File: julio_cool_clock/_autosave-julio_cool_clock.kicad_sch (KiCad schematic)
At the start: 60 parts, among them J1 PJ-102AH, J2 Conn_02x03_Odd_Even, J3 Conn_01x06, Q1 NPN_2N3904_SOT23, SW1 Omron_B3F_SPST, SW2 Omron_B3F_SPST, SW3 Omron_B3F_SPST, SW4 Omron_B3F_SPST, U1 ATmega328-PU, U2 MAX7219, U3 DS1307_DIP-8, U4 L7805, Y1 Crystal_16MHz, Y2 Crystal_32768Hz

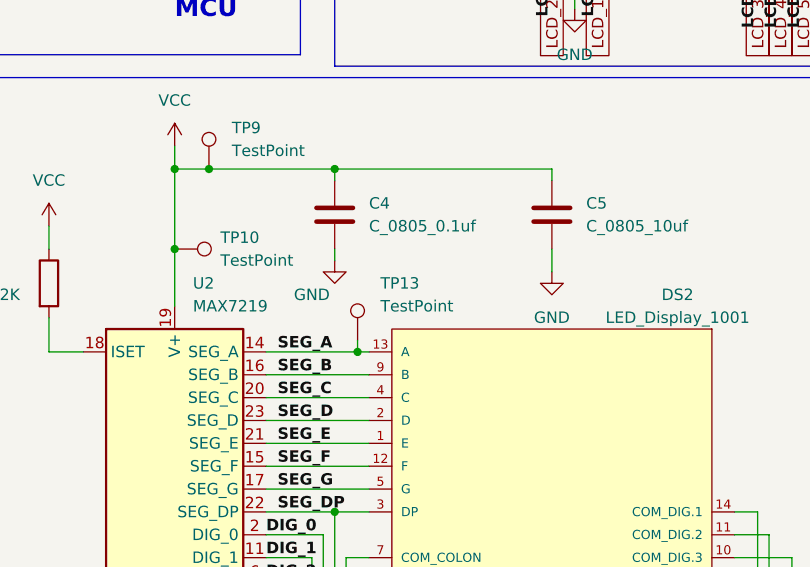
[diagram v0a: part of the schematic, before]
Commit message: Design Commit 6
Added prelim DFT features, completed PCB routing, and shipped first Gerber out.
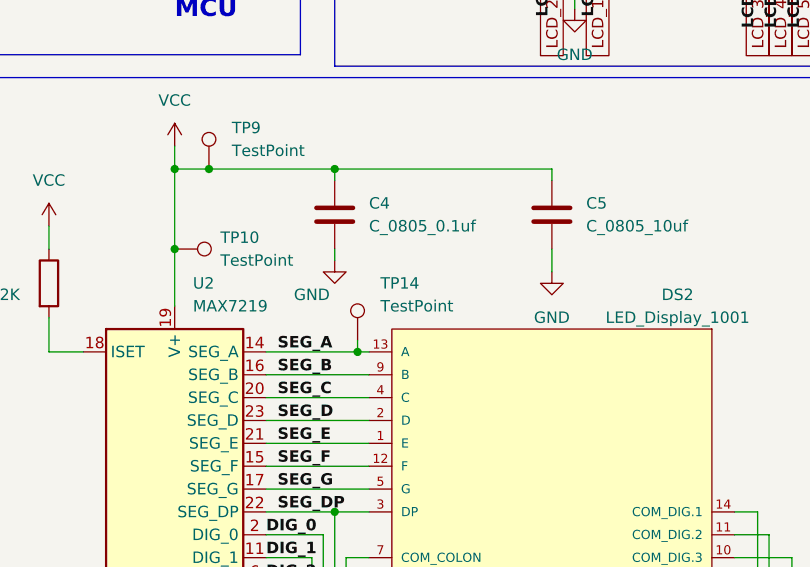
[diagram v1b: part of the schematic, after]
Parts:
- renumbered TP13 to TP14
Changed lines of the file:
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@@
   (symbol (lib_id "HPS:TestPoint") (at 113.03 143.51 0) (unit 1)
     (in_bom yes) (on_board yes)
-    (property "Reference" "TP13" (id 0) (at 115.57 137.16 0)
+    (property "Reference" "TP14" (id 0) (at 115.57 137.16 0)
       (effects (font (size 1.27 1.27)) (justify left))
     )
@@
       (reference "TP12") (unit 1) (value "TestPoint") (footprint "footprints:TestPoint_THTPad_D2.0mm_Drill1.0mm")
     )
-    (path "/18284de9-0621-4232-a79b-da0a3c7eb084"
-      (reference "TP13") (unit 1) (value "TestPoint") (footprint "footprints:TestPoint_THTPad_D2.0mm_Drill1.0mm")
-    )
     (path "/71840b63-43c6-4d29-b74e-3f6956efaa5c"
       (reference "TP13") (unit 1) (value "TestPoint") (footprint "footprints:TestPoint_THTPad_D2.0mm_Drill1.0mm")
     )
+    (path "/18284de9-0621-4232-a79b-da0a3c7eb084"
+      (reference "TP14") (unit 1) (value "TestPoint") (footprint "footprints:TestPoint_THTPad_D2.0mm_Drill1.0mm")
+    )
     (path "/a485a5d8-9902-4d0a-a13d-8b00d3d228d1"
